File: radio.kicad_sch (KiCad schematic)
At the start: 5 parts, among them J3 SMA_Coax, U11 RN2483

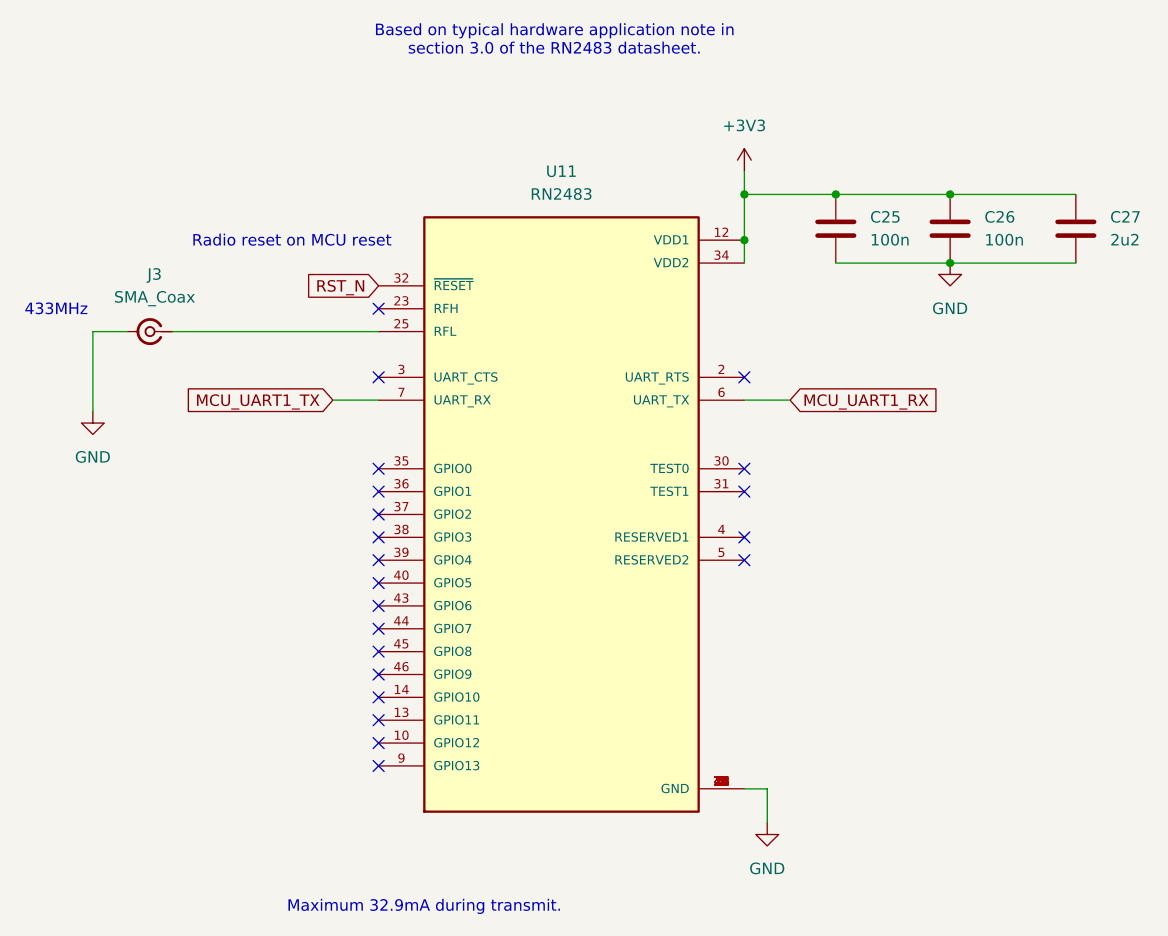
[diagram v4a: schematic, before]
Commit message: Update radio module to RN2903 for unlicensed band.
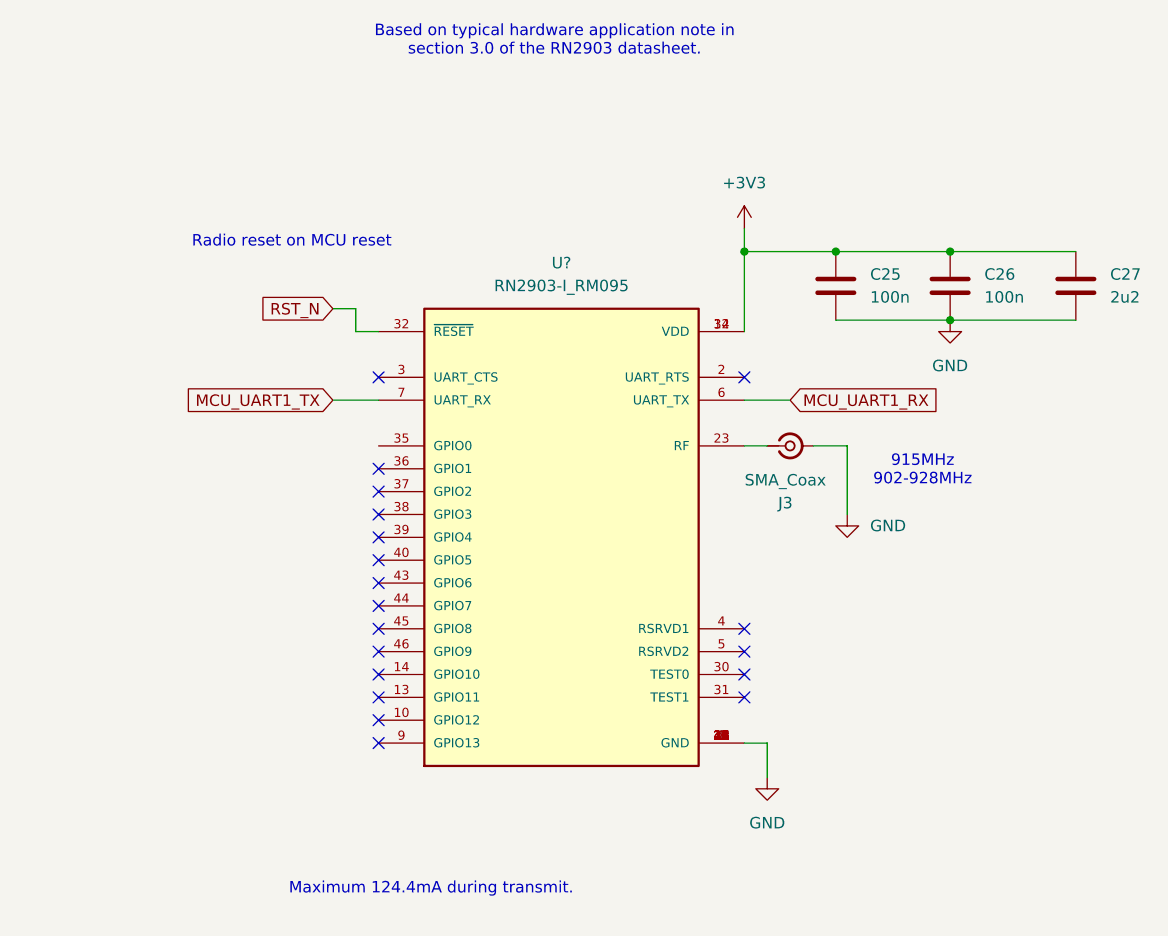
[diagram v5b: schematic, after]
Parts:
- removed U11: RN2483, RF_Module:RN2483, symbol RN2483:RN2483-I_RM095
- added U?: RN2903-I_RM095, RN2903-I_RM095:XCVR_RN2903-I_RM095, symbol RN2903:RN2903-I_RM095
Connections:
- net +3V3: now also U?.12 (VDD), U?.34 (VDD)
- net GND: now also U?.1 (GND), U?.11 (GND), U?.20 (GND), U?.21 (GND), U?.22 (GND), U?.24 (GND), U?.26 (GND), U?.27 (GND), U?.28 (GND), U?.33 (GND), U?.41 (GND), U?.47 (GND), U?.8 (GND)
- net MCU_UART1_RX: now also U?.6 (UART_TX)
- net MCU_UART1_TX: now also U?.7 (UART_RX)
- net RST_N: now also U?.32 (~{RESET})
- net at J3.1 (In): now also U?.23 (RF)
- no-connect marks 21 -> 19
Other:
- note added: "915MHz 902-928MHz"
- note added: "Based on typical hardware application note in section 3.0 of the RN2903 datasheet."
- note added: "Maximum 124.4mA during transmit."
- note removed: "433MHz"
- note removed: "Based on typical hardware application note in section 3.0 of the RN2483 datasheet."
- note removed: "Maximum 32.9mA during transmit."
- moved on the sheet: C25, C26, C27, J3

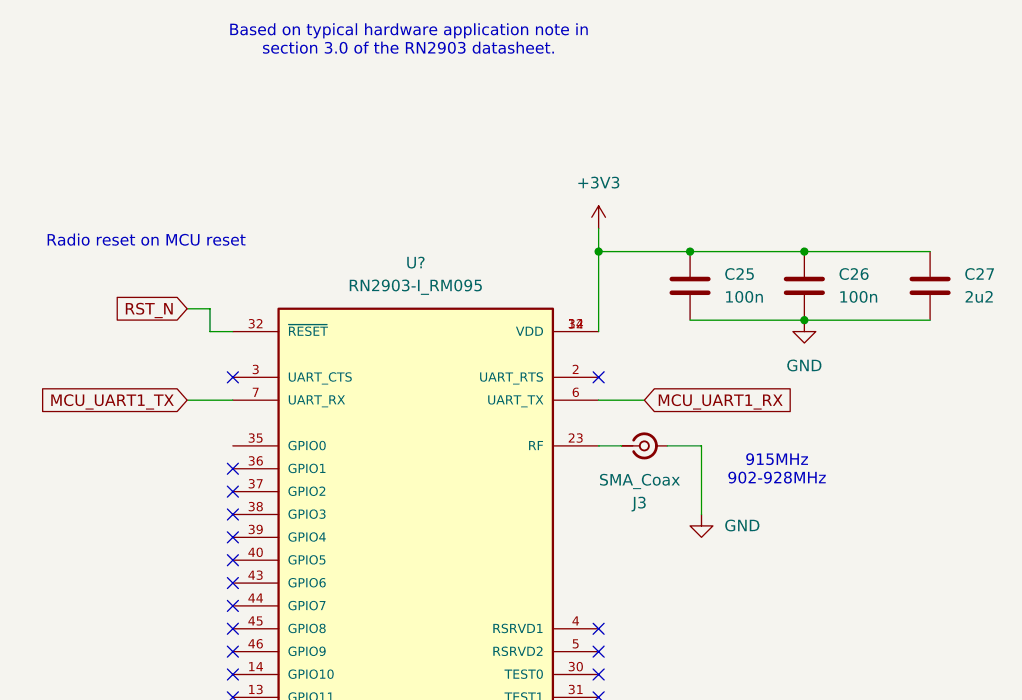
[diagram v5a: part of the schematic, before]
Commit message: Update net names.
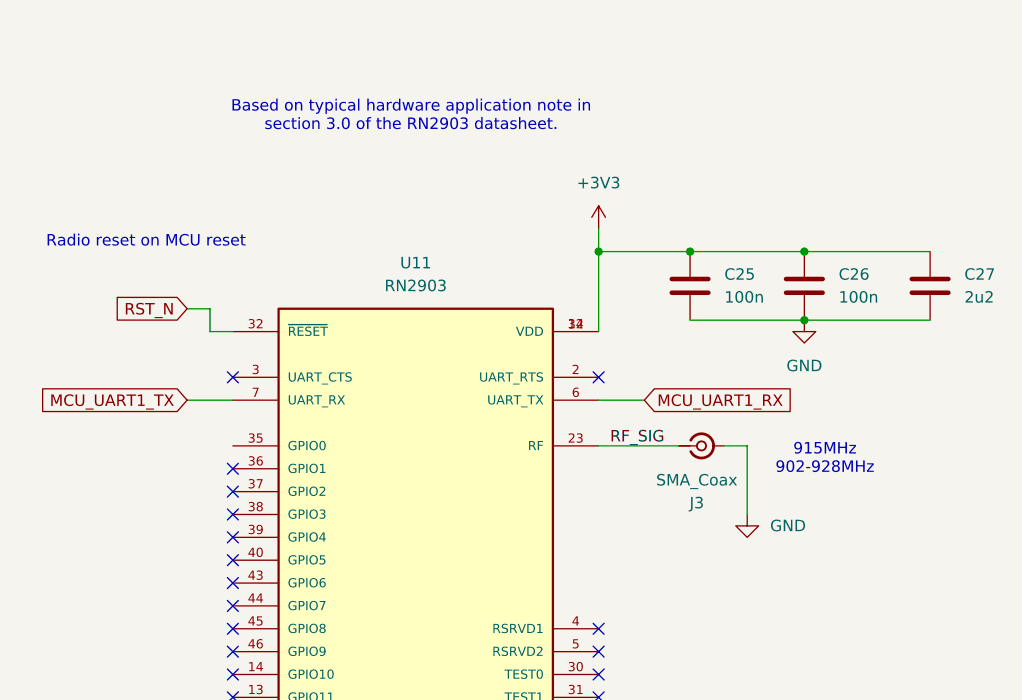
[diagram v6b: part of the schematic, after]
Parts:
- U11: renamed from U?; value RN2903-I_RM095 -> RN2903; footprint RN2903-I_RM095:XCVR_RN2903-I_RM095 -> RF_Module:RN2903
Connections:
- net RF_SIG: now reaches J3.1 (In), U11.23 (RF)
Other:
- moved on the sheet: J3
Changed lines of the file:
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@@
 	(wire
 		(pts
-			(xy 179.07 97.79) (xy 179.07 105.41)
+			(xy 184.15 97.79) (xy 184.15 105.41)
 		)
 		(stroke
@@
 	(wire
 		(pts
-			(xy 170.18 97.79) (xy 167.64 97.79)
+			(xy 176.53 97.79) (xy 167.64 97.79)
 		)
 		(stroke
@@
 	(wire
 		(pts
-			(xy 179.07 97.79) (xy 175.26 97.79)
+			(xy 184.15 97.79) (xy 181.61 97.79)
 		)
 		(stroke
@@
 	(text "915MHz\n902-928MHz\n"
 		(exclude_from_sim no)
-		(at 187.452 100.584 0)
+		(at 192.786 99.314 0)
 		(effects
 			(font
@@
 	(text "Based on typical hardware application note in\nsection 3.0 of the RN2903 datasheet."
 		(exclude_from_sim no)
-		(at 146.558 52.832 0)
+		(at 146.812 61.214 0)
 		(effects
 			(font
@@
 		)
 	)
+	(label "RF_SIG"
+		(at 168.91 97.79 0)
+		(fields_autoplaced yes)
+		(effects
+			(font
+				(size 1.27 1.27)
+			)
+			(justify left bottom)
+		)
+	)
 	(global_label "MCU_UART1_TX"
 		(shape input)
@@
 	(symbol
 		(lib_id "power:GND")
-		(at 179.07 105.41 0)
+		(at 184.15 105.41 0)
 		(unit 1)
 		(exclude_from_sim no)
@@
 		(fields_autoplaced yes)
 		(property "Reference" "#PWR059"
-			(at 179.07 111.76 0)
+			(at 184.15 111.76 0)
 			(effects
 				(font
@@
 		)
 		(property "Value" "GND"
-			(at 181.61 106.6799 0)
+			(at 186.69 106.6799 0)
 			(effects
 				(font
@@
 		)
 		(property "Footprint" ""
-			(at 179.07 105.41 0)
+			(at 184.15 105.41 0)
 			(effects
 				(font
@@
 		)
 		(property "Datasheet" ""
-			(at 179.07 105.41 0)
+			(at 184.15 105.41 0)
 			(effects
 				(font
@@
 		)
 		(property "Description" "Power symbol creates a global label with name \"GND\" , ground"
-			(at 179.07 105.41 0)
+			(at 184.15 105.41 0)
 			(effects
 				(font
@@
 		(dnp no)
 		(fields_autoplaced yes)
-		(property "Reference" "U?"
+		(property "Reference" "U11"
 			(at 147.32 77.47 0)
 			(effects
@@
 			)
 		)
-		(property "Value" "RN2903-I_RM095"
+		(property "Value" "RN2903"
 			(at 147.32 80.01 0)
 			(effects
@@
 			)
 		)
-		(property "Footprint" "RN2903-I_RM095:XCVR_RN2903-I_RM095"
+		(property "Footprint" "RF_Module:RN2903"
 			(at 147.32 107.95 0)
 			(effects
@@
 			(project ""
 				(path "/b90d3133-97a4-4747-8a68-e80f353c7b97/4aee52ff-1633-42f1-aa90-3806408b7a97"
-					(reference "U?")
+					(reference "U11")
 					(unit 1)
 				)
@@
 	(symbol
 		(lib_id "Connector:Conn_Coaxial_Small")
-		(at 172.72 97.79 0)
+		(at 179.07 97.79 0)
 		(unit 1)
 		(exclude_from_sim no)
@@
 		(fields_autoplaced yes)
 		(property "Reference" "J3"
-			(at 172.2005 104.14 0)
+			(at 178.5505 104.14 0)
 			(effects
 				(font
@@
 		)
 		(property "Value" "SMA_Coax"
-			(at 172.2005 101.6 0)
+			(at 178.5505 101.6 0)
 			(effects
 				(font
@@
 		)
 		(property "Footprint" "Connector_Coaxial:SMA_Molex_73251-1153_EdgeMount_Horizontal"
-			(at 172.72 97.79 0)
+			(at 179.07 97.79 0)
 			(effects
 				(font
@@
 		)
 		(property "Datasheet" "~"
-			(at 172.72 97.79 0)
+			(at 179.07 97.79 0)
 			(effects
 				(font
@@
 		)
 		(property "Description" "small coaxial connector (BNC, SMA, SMB, SMC, Cinch/RCA, LEMO, ...)"
-			(at 172.72 97.79 0)
-			(effects
-				(font
+			(at 179.07 97.79 0)
+			(effects
+				(font
